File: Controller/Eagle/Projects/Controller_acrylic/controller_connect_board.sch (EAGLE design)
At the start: 15 parts, among them J1 JST_3PIN_GND_VDD_SIG, J2 JST_3PIN_GND_VDD_SIG, J3 JST_3PIN_GND_VDD_SIG, J4 JST_3PIN_GND_VDD_SIG, J5 GIMBAL_3PIN_MATCH_TDOCU

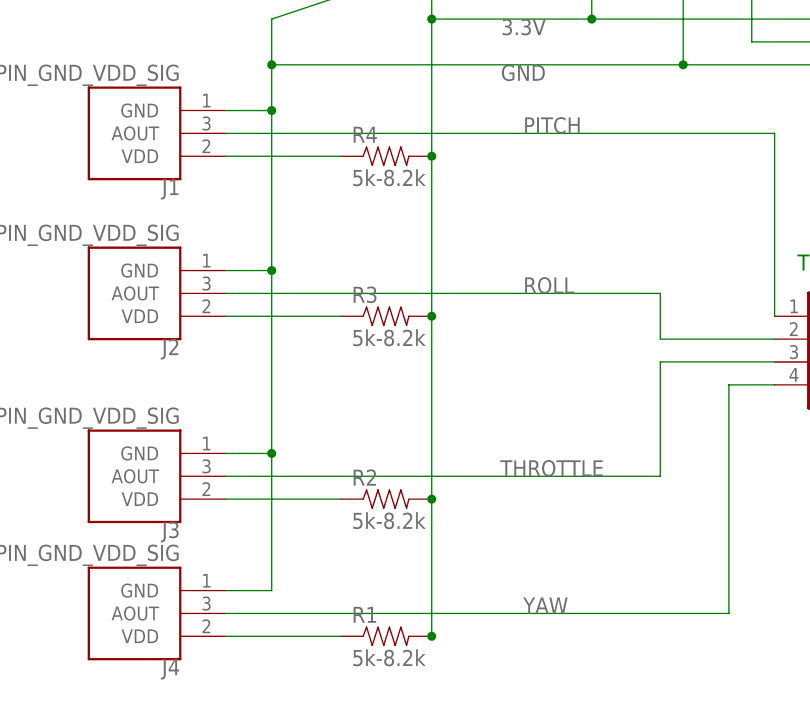
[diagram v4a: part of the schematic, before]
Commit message: Added dxf files Changed resistor values to 5.6k to be consistent with BOM
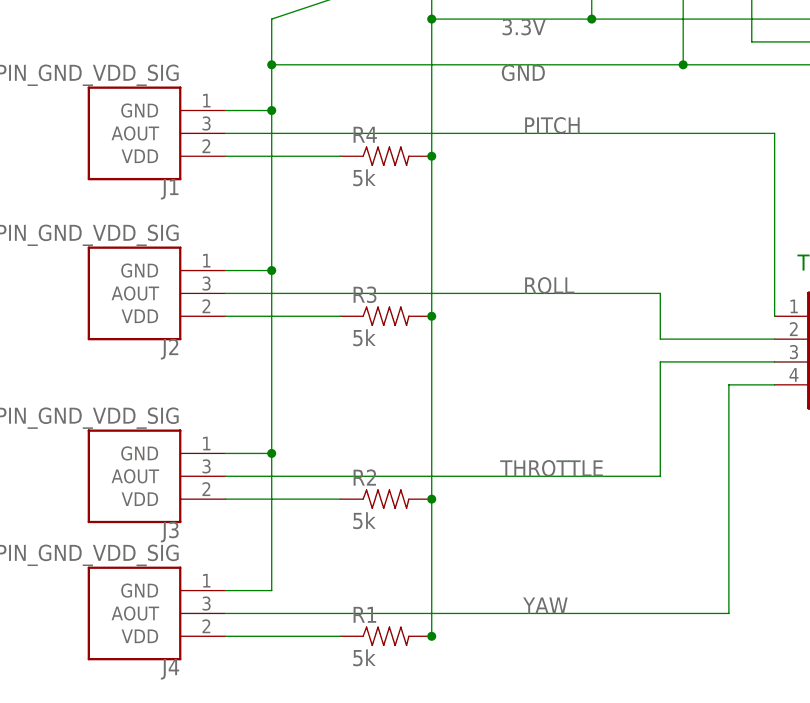
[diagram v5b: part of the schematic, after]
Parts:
- R1, R2, R3, R4: value 5k-8.2k -> 5k
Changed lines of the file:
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@@
 <part name="J3" library="Controller" deviceset="JST_3PIN_GND_VDD_SIG" device=""/>
 <part name="J4" library="Controller" deviceset="JST_3PIN_GND_VDD_SIG" device=""/>
-<part name="R1" library="SparkFun-Resistors" deviceset="RESISTOR" device="PTH-1/4W" value="5k-8.2k"/>
-<part name="R2" library="SparkFun-Resistors" deviceset="RESISTOR" device="PTH-1/4W" value="5k-8.2k"/>
-<part name="R3" library="SparkFun-Resistors" deviceset="RESISTOR" device="PTH-1/4W" value="5k-8.2k"/>
-<part name="R4" library="SparkFun-Resistors" deviceset="RESISTOR" device="PTH-1/4W" value="5k-8.2k"/>
+<part name="R1" library="SparkFun-Resistors" deviceset="RESISTOR" device="PTH-1/4W" value="5k"/>
+<part name="R2" library="SparkFun-Resistors" deviceset="RESISTOR" device="PTH-1/4W" value="5k"/>
+<part name="R3" library="SparkFun-Resistors" deviceset="RESISTOR" device="PTH-1/4W" value="5k"/>
+<part name="R4" library="SparkFun-Resistors" deviceset="RESISTOR" device="PTH-1/4W" value="5k"/>
 <part name="JP6" library="SparkFun-Connectors" deviceset="M04" device="PTH"/>
 <part name="JP1" library="SparkFun-Connectors" deviceset="M02" device="1X02_NO_SILK"/>
